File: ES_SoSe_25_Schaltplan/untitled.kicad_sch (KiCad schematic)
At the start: 0 parts

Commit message: updated scematic
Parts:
- added A2: Clone_Mega2560_Pro_Socket, PCM_arduino-library:Clone_Mega2560_Pro_Socket, symbol arduino-library:Clone_Mega2560_Pro_Socket
- added A3: Arduino_Nano_33_BLE_Sense_Tile, PCM_arduino-library:Arduino_Nano_Every_Tile, symbol arduino-library:Arduino_Nano_33_BLE_Sense_Tile
- added D2: LED_Blue, symbol Device:LED
- added R2: 180R, symbol Device:R
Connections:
- new net: A2.D18 (D18/TX1), A3.D0 (D0/RX)
- new net: A2.D19 (D19/RX1), A3.D1 (D1/TX)
- new net: A3.D4, R2.1
- new net: D2.2 (A), R2.2
- new net GND: A2.GND1 (GND), A2.GND2 (GND), A3.GND1 (GND), A3.GND2 (GND), D2.1 (K)
- new net VCC: A2.VIN1 (VIN), A3.VIN
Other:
- note added: "BLE Connection Status"

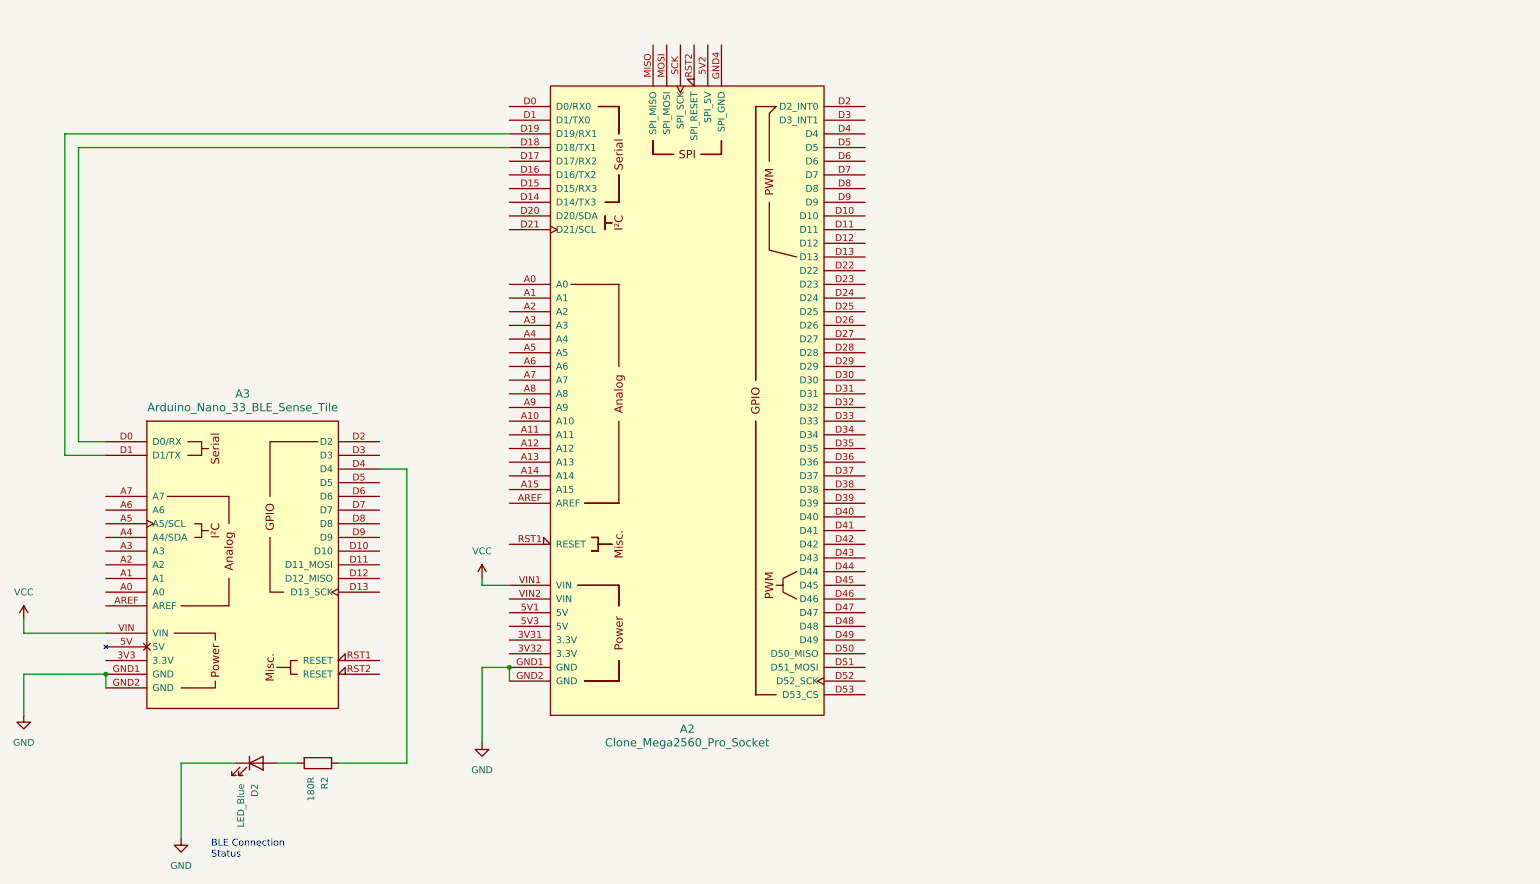
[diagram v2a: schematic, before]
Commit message: updated scematic and added UART LED
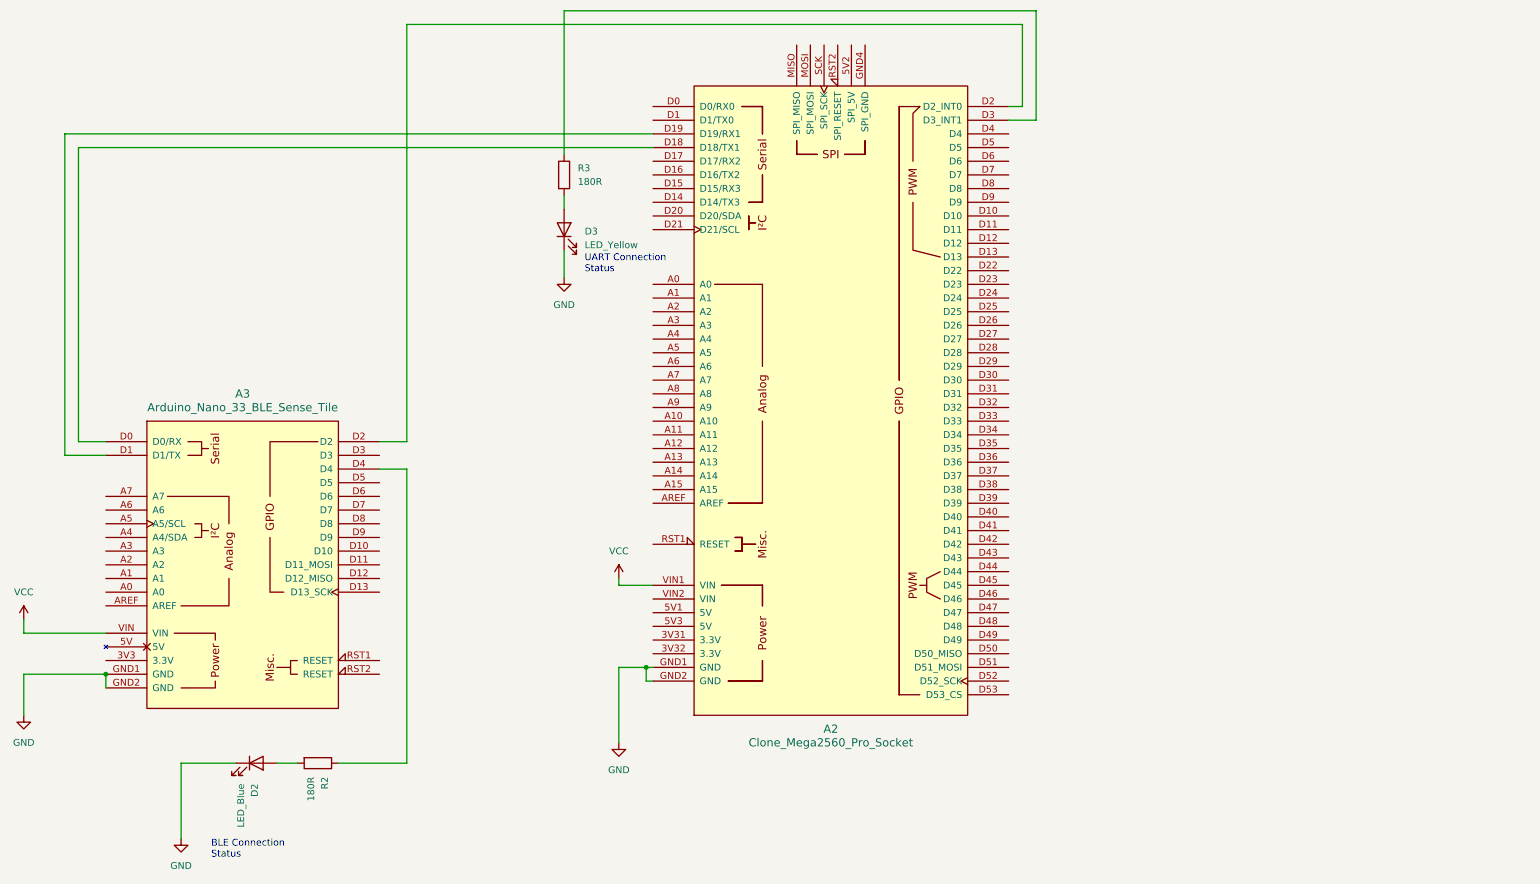
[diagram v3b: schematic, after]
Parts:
- added D3: LED_Yellow, symbol Device:LED
- added R3: 180R, symbol Device:R
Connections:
- net GND: now also D3.1 (K)
- net at A3.D2: now also A2.D2 (D2_INT0)
- net at A2.D3 (D3_INT1): now also R3.1
- new net: D3.2 (A), R3.2
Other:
- note added: "UART Connection Status"
- moved on the sheet: A2

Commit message: Motor und H-Brücke im Schaltplan eingefügt
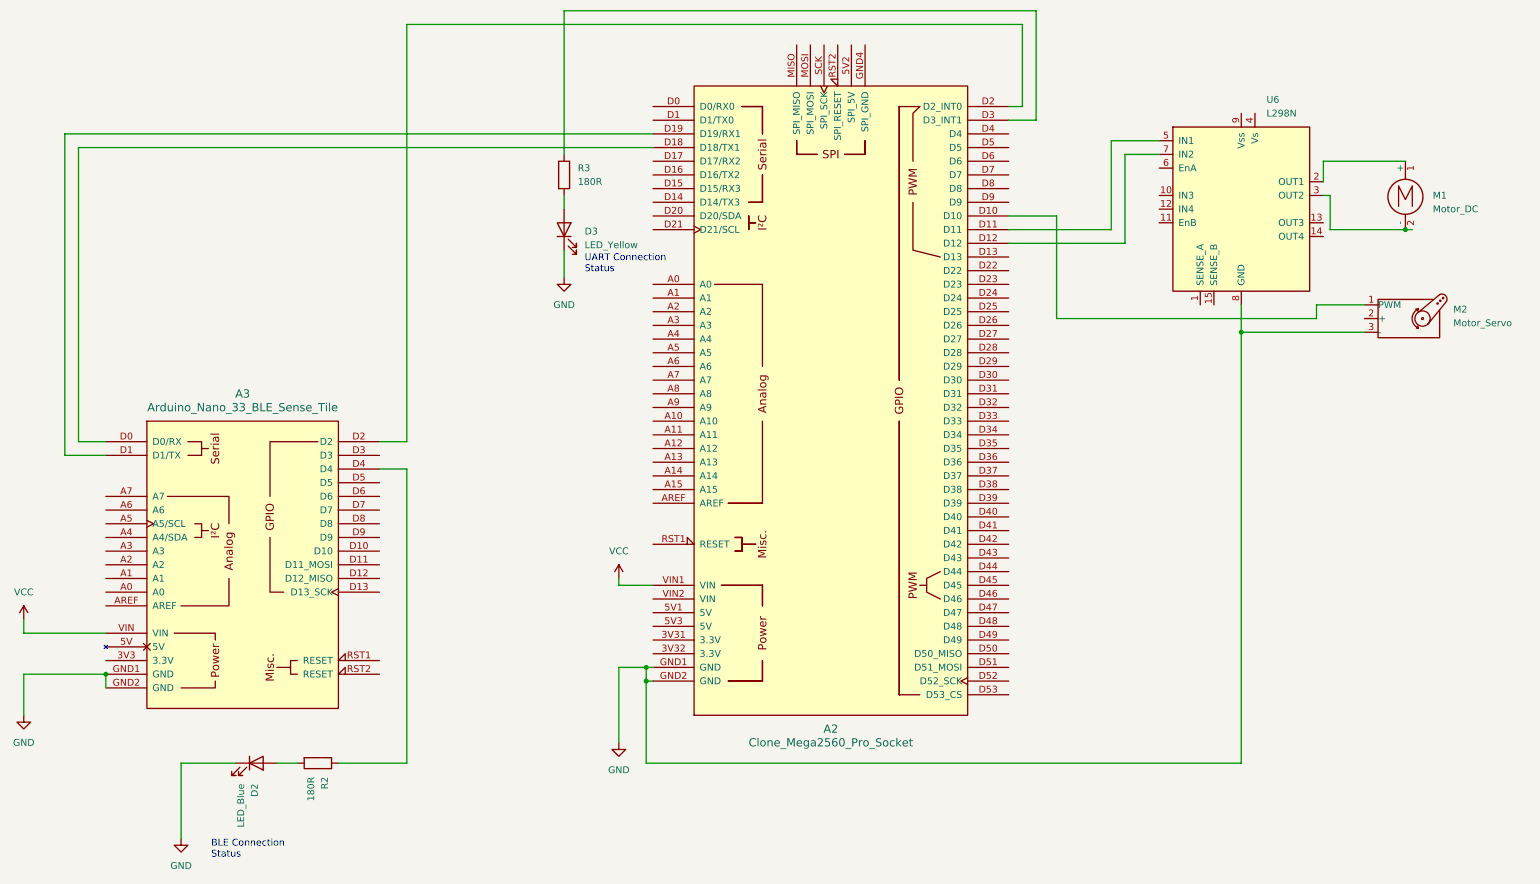
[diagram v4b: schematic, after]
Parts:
- added M1: Motor_DC, symbol Motor:Motor_DC
- added M2: Motor_Servo, symbol Motor:Motor_Servo
- added U6: L298N, Package_TO_SOT_THT:TO-220-15_P2.54x2.54mm_StaggerOdd_Lead4.58mm_Vertical, symbol Driver_Motor:L298N
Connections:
- net GND: now also M2.3 (-), U6.8 (GND)
- net at A2.D10: now also M2.1 (PWM)
- net at A2.D11: now also U6.5 (IN1)
- net at A2.D12: now also U6.7 (IN2)
- new net: M1.1 (+), U6.2 (OUT1)
- new net: M1.2 (-), U6.3 (OUT2)

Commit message: changed mega pins
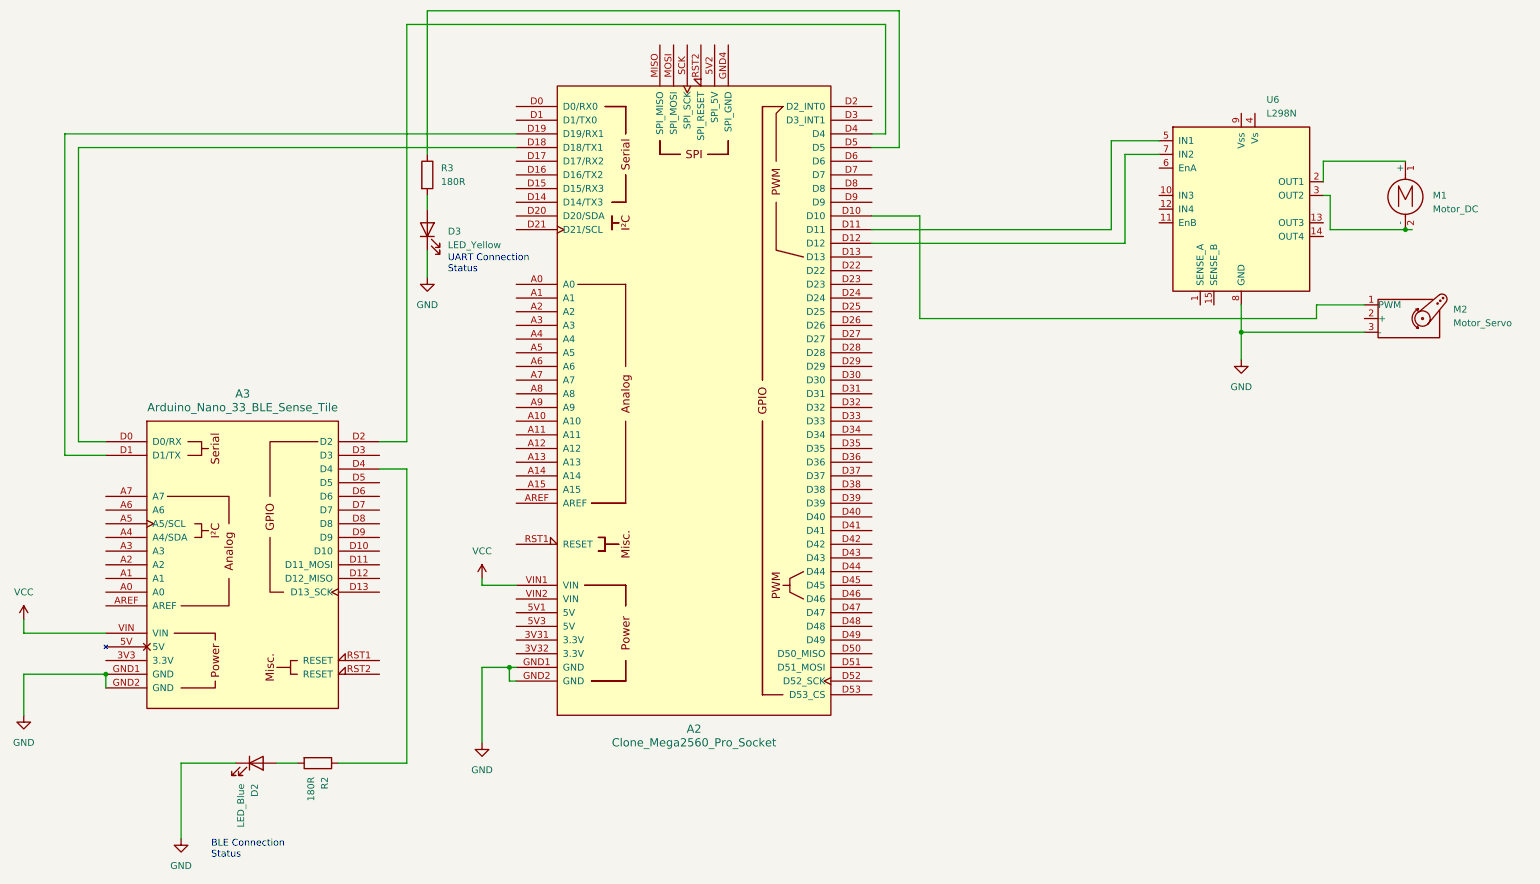
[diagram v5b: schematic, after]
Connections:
- net at A3.D2: now also A2.D4; no longer A2.D2 (D2_INT0)
- net at R3.1: now also A2.D5; no longer A2.D3 (D3_INT1)
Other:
- moved on the sheet: A2, D3, R3

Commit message: Schaltplan Vollständig Jan
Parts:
- added BT1: Battery, symbol Device:Battery
- added U7, U8: LM2596S-3.3, Package_TO_SOT_SMD:TO-263-5_TabPin3, symbol Regulator_Switching:LM2596S-3.3
- added U9: TSSP58038SS1XB, OptoDevice:Vishay_MINICAST-3Pin, symbol Sensor_Proximity:TSSP58038SS1XB
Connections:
- net GND: now also BT1.2 (-), U7.2 (OUT), U7.3 (GND), U7.5 (~{ON}/OFF), U8.2 (OUT), U8.3 (GND), U8.5 (~{ON}/OFF), U9.2 (GND)
- net at A2.5V1 (5V): now also U9.3 (Vs)
- net at A2.D2 (D2_INT0): now also U9.1 (OUT)
- net at M2.2 (+): now also U8.4 (FB)
- net at U6.9 (Vss): now also U7.4 (FB)
- new net: BT1.1 (+), U7.1 (VIN), U8.1 (VIN)
